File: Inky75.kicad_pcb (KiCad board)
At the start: 2 copper layers, 309.5 x 152.1 mm, 193 parts, among them J1 J, K1 K, M1 M, P1 P, Q1 Q, T1 T, U1 KB2040, U2 U, X1 X, Y1 Y

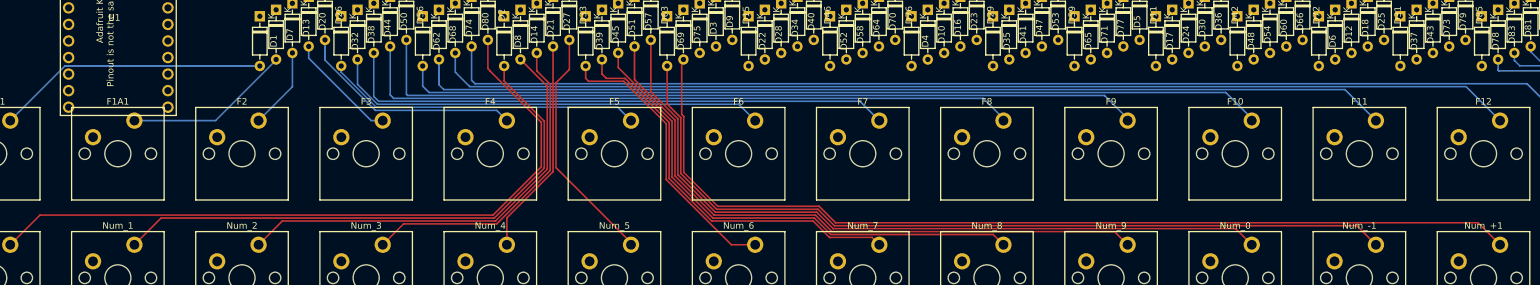
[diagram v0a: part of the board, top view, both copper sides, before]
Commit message: started tidying traces
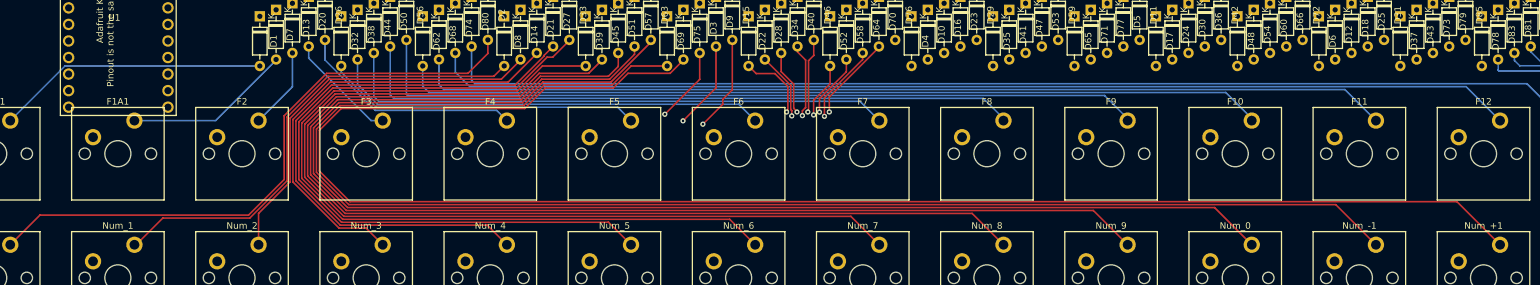
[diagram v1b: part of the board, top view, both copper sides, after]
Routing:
- net Net-(D75-Pad2): track 147.4 -> 252.5 mm
- net Net-(D69-Pad2): track 128.5 -> 231.6 mm
- net Net-(D63-Pad2): track 114.9 -> 213.0 mm
- net Net-(D57-Pad2): track 96.3 -> 192.7 mm
- net Net-(D51-Pad2): track 77.6 -> 172.4 mm
- net Net-(D45-Pad2): track 60.7 -> 150.4 mm
- net Net-(D39-Pad2): track 43.5 -> 129.5 mm
- net Net-(D33-Pad2): track 37.0 -> 110.7 mm
- net Net-(D27-Pad2): track 33.4 -> 89.9 mm
- net Net-(D21-Pad2): track 49.3 -> 69.0 mm
- net Net-(D2-Pad2): track 109.3 -> 93.2 mm
- net Net-(D15-Pad2): track 0.00 -> 14.8 mm, vias 0 -> 1
- net Net-(D9-Pad2): track 0.00 -> 13.5 mm, vias 0 -> 1
- net Net-(D70-Pad2): track 0.00 -> 13.2 mm, vias 0 -> 1
- net Net-(D64-Pad2): track 0.00 -> 12.1 mm, vias 0 -> 1
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
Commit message: fixing traces
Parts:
- removed the D43 at (292.1, 78.7)
- added D78: 1N4148, Diode_THT:D_DO-35_SOD27_P7.62mm_Horizontal, F.Cu at (277.1, 79.7)
- moved D31 4.72 mm to (289.6, 79.7)
- moved D12 2.69 mm to (282.1, 77.7)
- moved D18 2.69 mm to (284.6, 76.7)
- moved D25 2.69 mm to (287.1, 75.7)
- moved D37 2.69 mm to (292.1, 78.7)
- moved D6 2.69 mm to (279.6, 78.7)
- renumbered D73 to D43, D79 to D73, D85 to D79, D78 to D85
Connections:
- D43 pad 2: Net-(D73-Pad2) -> Net-(D43-Pad2)
- D46 pad 1: unconnected-(D46-Pad1) -> Row_3
- D46 pad 2: unconnected-(D46-Pad2) -> Net-(D46-Pad2)
- D73 pad 2: Net-(D79-Pad2) -> Net-(D73-Pad2)
- D79 pad 2: Net-(D85-Pad2) -> Net-(D79-Pad2)
- D85 pad 1: Row_5 -> Row_6
- D85 pad 2: Net-(D78-Pad2) -> Net-(D85-Pad2)
- U2 pad 2: unconnected-(U2-Pad2) -> Net-(D46-Pad2)
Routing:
- net Col_11: track 0.00 -> 359.1 mm, vias 0 -> 1
- net Col_14: track 0.00 -> 330.8 mm
- net Net-(D6-Pad2): track 2.38 -> 332.6 mm, vias 0 -> 2
- net Net-(D12-Pad2): track 7.14 -> 308.5 mm, vias 0 -> 2
- net Net-(D5-Pad2): track 0.00 -> 296.3 mm, vias 0 -> 2
- net Col_9: track 0.00 -> 293.1 mm, vias 0 -> 1
- net Col_13: track 0.00 -> 279.3 mm
- net Net-(D18-Pad2): track 9.52 -> 282.9 mm, vias 0 -> 2
- net Net-(D11-Pad2): track 0.00 -> 268.7 mm, vias 0 -> 2
- net Col_10: track 0.00 -> 259.0 mm, vias 0 -> 1
- net Col_8: track 0.00 -> 250.9 mm, vias 0 -> 1
- net Net-(D17-Pad2): track 0.00 -> 249.0 mm, vias 0 -> 2
- net Net-(C1-Pad2): track 0.00 -> 232.5 mm, vias 0 -> 2
- net Col_7: track 0.00 -> 231.0 mm
- net Net-(D30-Pad2): track 0.00 -> 216.0 mm, vias 0 -> 2
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
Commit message: finished routing traces
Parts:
- removed U$1, U$17, U$19, U$21: MOUNTINGHOLE2.5, Adafruit 1.3in 128x64 OLED STEMMA QT:MOUNTINGHOLE_2.5_PLATED
- removed U$25: , Adafruit 1.3in 128x64 OLED STEMMA QT:PCBFEAT-REV-040
- removed U1: KB2040, kb2040_NEW:KB2040_FINAAL
- added J2: helios_border, 0xCB-HeliosFootprint:helios_border, F.Cu at (93.4, 74.9)
- moved D1 2.36 mm to (114.6, 77.4)
- moved D10 2.36 mm to (222.1, 74.4)
- moved D11 2.36 mm to (257.1, 75.4)
- moved D12 2.36 mm to (294.6, 75.4)
- moved D13 2.36 mm to (119.6, 75.4)
- moved D14 2.36 mm to (154.6, 76.4)
- moved D15 2.36 mm to (189.6, 77.4)
- moved D16 2.36 mm to (224.6, 73.4)
- moved D17 2.36 mm to (259.6, 74.4)
- moved D18 2.36 mm to (297.1, 74.4)
- moved D2 2.36 mm to (149.6, 73.4)
- moved D20 2.36 mm to (122.1, 74.4)
- moved D21 2.36 mm to (157.1, 75.4)
- moved D22 2.36 mm to (192.1, 76.4)
- moved D23 2.36 mm to (227.1, 77.4)
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- renumbered D23 to D10, D30 to D11, D43 to D12, D22 to D15, D29 to D16, D36 to D17, D73 to D18, D28 to D22, D35 to D23, D42 to D24, D79 to D25, D34 to D28, D41 to D29, D9 to D3, D48 to D30, D85 to D31, D40 to D34, D47 to D35, D54 to D36, D83 to D37, D16 to D4, D46 to D40, D53 to D41, D60 to D42, D81 to D43, D52 to D46, D59 to D47, D66 to D48, D84 to D49, D24 to D5, D58 to D52, D65 to D53, D72 to D54, D67 to D55, D64 to D58, D71 to D59, D37 to D6, D78 to D60, D31 to D61, D70 to D64, D77 to D65, D6 to D66, D61 to D67, D76 to D70, D5 to D71, D12 to D72, D82 to D73, D4 to D76, D11 to D77, D18 to D78, D49 to D79, D17 to D81, D10 to D82, D3 to D83, D25 to D84, D55 to D85, D15 to D9
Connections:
- D10 pad 2: Net-(D19-Pad2) -> Net-(A1-Pad2)
- D11 pad 2: Net-(D30-Pad2) -> Net-(D11-Pad2)
- D12 pad 2: Net-(D43-Pad2) -> Net-(D12-Pad2)
- D15 pad 2: Net-(D22-Pad2) -> Net-(D15-Pad2)
- D16 pad 2: Net-(D29-Pad2) -> Net-(D16-Pad2)
- D17 pad 2: Net-(B1-Pad2) -> Net-(D17-Pad2)
- D18 pad 2: Net-(D73-Pad2) -> Net-(D18-Pad2)
- D22 pad 2: Net-(D28-Pad2) -> Net-(D22-Pad2)
- D23 pad 2: Net-(D35-Pad2) -> Net-(D19-Pad2)
- D24 pad 2: Net-(D42-Pad2) -> Net-(C1-Pad2)
- D25 pad 2: Net-(D79-Pad2) -> Net-(D25-Pad2)
- D28 pad 2: Net-(D34-Pad2) -> Net-(D28-Pad2)
- D29 pad 2: Net-(D41-Pad2) -> Net-(D29-Pad2)
- D3 pad 2: Net-(D9-Pad2) -> Net-(D3-Pad2)
- D30 pad 2: Net-(D48-Pad2) -> Net-(D30-Pad2)
- D31 pad 2: Net-(D85-Pad2) -> Net-(D31-Pad2)
- D34 pad 2: Net-(D40-Pad2) -> Net-(D34-Pad2)
- D35 pad 2: Net-(D47-Pad2) -> Net-(D35-Pad2)
- D36 pad 2: Net-(<1-Pad2) -> Net-(B1-Pad2)
- D37 pad 1: Row_2 -> Row_6
- D37 pad 2: Net-(BACKSPACE1-Pad2) -> Net-(D37-Pad2)
- D4 pad 2: Net-(D16-Pad2) -> Net-(Caps1-Pad2)
- D40 pad 2: Net-(D46-Pad2) -> Net-(D40-Pad2)
- D41 pad 2: Net-(D53-Pad2) -> Net-(D41-Pad2)
- D42 pad 2: Net-(>1-Pad2) -> Net-(D42-Pad2)
- D43 pad 1: Row_4 -> Row_6
- D43 pad 2: Net-(D81-Pad2) -> Net-(D43-Pad2)
- D46 pad 2: Net-(D52-Pad2) -> Net-(D46-Pad2)
- D47 pad 2: Net-(D59-Pad2) -> Net-(D47-Pad2)
- D48 pad 2: Net-(/1-Pad2) -> Net-(D48-Pad2)
- D49 pad 1: Row_5 -> Row_6
- D49 pad 2: Net-(D84-Pad2) -> Net-(D49-Pad2)
- D5 pad 2: Net-(C1-Pad2) -> Net-(D5-Pad2)
- D52 pad 2: Net-(D58-Pad2) -> Net-(D52-Pad2)
- D53 pad 2: Net-(;1-Pad2) -> Net-(D53-Pad2)
- D54 pad 2: Net-(D72-Pad2) -> Net-(<1-Pad2)
- D55 pad 2: Net-(D67-Pad2) -> Net-(D55-Pad2)
- D58 pad 2: Net-(D64-Pad2) -> Net-(D58-Pad2)
- D59 pad 2: Net-('1-Pad2) -> Net-(D59-Pad2)
- D6 pad 2: Net-(D37-Pad2) -> Net-(D6-Pad2)
- D60 pad 2: Net-(D78-Pad2) -> Net-(>1-Pad2)
- D61 pad 2: Net-(D31-Pad2) -> Net-(D61-Pad2)
- D64 pad 2: Net-(D70-Pad2) -> Net-(D64-Pad2)
- D65 pad 2: Net-(D77-Pad2) -> Net-(;1-Pad2)
- D66 pad 1: Row_6 -> Row_5
- D66 pad 2: Net-(D6-Pad2) -> Net-(/1-Pad2)
- D67 pad 2: Net-(D61-Pad2) -> Net-(D67-Pad2)
- D70 pad 2: Net-(D76-Pad2) -> Net-(D70-Pad2)
- D71 pad 1: Row_5 -> Row_4
- D71 pad 2: Net-(D5-Pad2) -> Net-('1-Pad2)
- D72 pad 1: Row_6 -> Row_5
- D72 pad 2: Net-(D12-Pad2) -> Net-(D72-Pad2)
- D73 pad 1: Row_3 -> Row_6
- D73 pad 2: Net-(D82-Pad2) -> Net-(D73-Pad2)
- D76 pad 1: Row_4 -> Row_3
- D76 pad 2: Net-(Caps1-Pad2) -> Net-(D76-Pad2)
- D77 pad 1: Row_5 -> Row_4
- D77 pad 2: Net-(D11-Pad2) -> Net-(D77-Pad2)
- D78 pad 1: Row_6 -> Row_5
- D78 pad 2: Net-(D18-Pad2) -> Net-(D78-Pad2)
- D79 pad 2: Net-(D49-Pad2) -> Net-(D79-Pad2)
- D81 pad 1: Row_5 -> Row_4
- D81 pad 2: Net-(D17-Pad2) -> Net-(D81-Pad2)
- D82 pad 1: Row_4 -> Row_3
- D82 pad 2: Net-(A1-Pad2) -> Net-(D82-Pad2)
- D83 pad 1: Row_3 -> Row_2
- D83 pad 2: Net-(D3-Pad2) -> Net-(BACKSPACE1-Pad2)
- D84 pad 1: Row_6 -> Row_5
- D84 pad 2: Net-(D25-Pad2) -> Net-(D84-Pad2)
- D85 pad 2: Net-(D55-Pad2) -> Net-(D85-Pad2)
- D9 pad 2: Net-(D15-Pad2) -> Net-(D9-Pad2)
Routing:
- net Net-(BACKSPACE1-Pad2): track 49.3 -> 285.2 mm
- net Row_6: track 30.5 -> 234.1 mm
- net Col_10: track 259.0 -> 424.6 mm, vias 1 -> 2
- net Col_12: track 153.3 -> 312.0 mm, vias 0 -> 1
- net Row_5: track 41.3 -> 194.2 mm
- net Col_8: track 250.9 -> 376.9 mm, vias 1 -> 2
- net Net-(D81-Pad2): track 78.9 -> 204.1 mm, vias 0 -> 2
- net Row_4: track 39.2 -> 158.7 mm
- net Col_9: track 293.1 -> 402.1 mm, vias 1 -> 2
- net Net-(D82-Pad2): track 38.6 -> 130.8 mm
- net Col_11: track 359.1 -> 444.4 mm, vias 1 -> 2
- net Row_3: track 39.2 -> 124.2 mm
- net Col_14: track 330.8 -> 386.0 mm, vias 0 -> 1
- net Col_13: track 279.3 -> 332.5 mm, vias 0 -> 1
- net Row_2: track 41.3 -> 91.7 mm
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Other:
- board size 309.5 x 152.1 mm -> 309.5 x 146 mm

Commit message: updated traces
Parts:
- removed the ? at (368.3, 92.1)
- removed L_ALT1.5u1: L_ALT_1.5u, Switch_Keyboard_Cherry_MX:SW_Cherry_MX_PCB_1.50u
- removed L_CTRL1: L_CTRL, Switch_Keyboard_Cherry_MX:SW_Cherry_MX_PCB_1.25u
- removed L_SUPER_1.5u1: L_SUPER_1.5u, Switch_Keyboard_Cherry_MX:SW_Cherry_MX_PCB_1.50u
- removed the REF** at (350.0, 110.3)
- removed the REF** at (350.0, 148.4)
- removed R_SPACEBAR2_2.75u1: R_SPACEBAR2_2.75u, Switch_Keyboard_Cherry_MX:SW_Cherry_MX_PCB_2.75u
- added D49: 1N4148, Diode_THT:D_DO-35_SOD27_P7.62mm_Horizontal, F.Cu at (324.6, 73.4)
- added REF**: Stabilizer_Cherry_MX_2.00u, Mounting_Keyboard_Stabilizer:Stabilizer_Cherry_MX_2.00u, F.Cu at (166.7, 196.0)
- added REF**: Stabilizer_Cherry_MX_3.00u, Mounting_Keyboard_Stabilizer:Stabilizer_Cherry_MX_3.00u, F.Cu at (169.1, 196.0)
- added REF**: Stabilizer_Cherry_MX_3.00u, Mounting_Keyboard_Stabilizer:Stabilizer_Cherry_MX_3.00u, F.Cu at (226.2, 196.0)
- added REF**: Stabilizer_Cherry_MX_6.00u, Mounting_Keyboard_Stabilizer:Stabilizer_Cherry_MX_6.00u, F.Cu at (197.6, 196.0)
- added REF**: Stabilizer_Cherry_MX_2.00u, Mounting_Keyboard_Stabilizer:Stabilizer_Cherry_MX_2.00u, F.Cu at (85.7, 177.0)
- added REF**: Stabilizer_Cherry_MX_2.00u, Mounting_Keyboard_Stabilizer:Stabilizer_Cherry_MX_2.00u, F.Cu at (331.0, 119.8)
- added REF**: Stabilizer_Cherry_MX_2.00u, Mounting_Keyboard_Stabilizer:Stabilizer_Cherry_MX_2.00u, F.Cu at (235.7, 196.0)
- added REF**: Stabilizer_Cherry_MX_2.00u, Mounting_Keyboard_Stabilizer:Stabilizer_Cherry_MX_2.00u, F.Cu at (338.1, 148.4)
- added R_SPACEBAR2_2.00u1: R_SPACEBAR2_2.00u1, Switch_Keyboard_Cherry_MX:SW_Cherry_MX_PCB_2.00u, F.Cu at (235.7, 196.0)
- added SPACEBAR1_1.25u3: SPACEBAR1_1.25u3, Switch_Keyboard_Cherry_MX:SW_Cherry_MX_PCB_1.25u, F.Cu at (204.8, 196.0)
- added SW1: SW_Push, Button_Switch_SMD:SW_SPST_TL3342, B.Cu at (110.3, 67.5)
- J2: value helios_border -> helios; footprint 0xCB-HeliosFootprint:helios_border -> 0xCB-HeliosFootprint:helios_no_GP_25
- L_ALT1: footprint Switch_Keyboard_Cherry_MX:SW_Cherry_MX_PCB_1.25u -> Switch_Keyboard_Cherry_MX:SW_Cherry_MX_PCB_1.00u
- L_SPACEBAR1: value L_SPACEBAR -> L_SPACEBAR_1_3u
- SPACEBAR_2: value SPACEBAR_2 -> SPACEBAR_2_3u
- moved L_SPACEBAR1_2.75u1 9.52 mm to (166.7, 196.0)
- moved ? 5.56 mm to (65.1, 59.5)
- moved REF** 5.56 mm to (65.1, 59.5)
- moved L_ALT1 2.38 mm to (102.4, 196.0)
- moved J2 0.34 mm to (93.4, 74.6)
- renumbered D37 to D31, D43 to D37, D73 to D43, D49 to D55, D55 to D67, D79 to D73, D85 to D79, D67 to D85, D31 to D86
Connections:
- D31 pad 2: Net-(D37-Pad2) -> Net-(D31-Pad2)
- D37 pad 2: Net-(D43-Pad2) -> Net-(D37-Pad2)
- D43 pad 2: Net-(D73-Pad2) -> Net-(D43-Pad2)
- D55 pad 2: Net-(D49-Pad2) -> Net-(D55-Pad2)
- D67 pad 2: Net-(D55-Pad2) -> Net-(D67-Pad2)
- D73 pad 2: Net-(D79-Pad2) -> Net-(D73-Pad2)
- D79 pad 2: Net-(D85-Pad2) -> Net-(D79-Pad2)
- D85 pad 2: Net-(D67-Pad2) -> Net-(D85-Pad2)
- D86 pad 2: Net-(D31-Pad2) -> Net-(D86-Pad2)
- J2 pad 10: Row_3 -> Col_13
- J2 pad 11: Row_2 -> Col_12
- J2 pad 12: Row_1 -> Col_11
- J2 pad 13: Col_1 -> Col_10
- J2 pad 14: Col_2 -> Col_9
- J2 pad 15: Col_3 -> Col_8
- J2 pad 16: Col_14 -> Col_7
- J2 pad 17: Col_13 -> Col_6
- J2 pad 18: Col_12 -> Col_5
- J2 pad 19: Col_11 -> Col_4
- J2 pad 20: Col_10 -> Col_15
- J2 pad 21: Col_9 -> Row_1
- J2 pad 22: Col_8 -> Row_2
- J2 pad 23: Col_7 -> Row_3
- J2 pad 24: Col_6 -> Row_4
- J2 pad 25: Col_5 -> Row_5
- J2 pad 26: Col_4 -> Row_6
- J2 pad 28: unconnected-(J2-Pad28) -> RST
- J2 pad 29: unconnected-(J2-Pad29) -> GND
- J2 pad 6: unconnected-(J2-Pad6) -> Col_1
- J2 pad 7: Row_6 -> Col_2
- J2 pad 8: Row_5 -> Col_3
- J2 pad 9: Row_4 -> Col_14
- SPACEBAR1_6u1 pad 1: Col_4 -> Col_15
- SPACEBAR1_6u1 pad 2: Net-(D25-Pad2) -> Net-(D86-Pad2)
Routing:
- net Net-(D86-Pad2): track 0.00 -> 216.5 mm, vias 0 -> 2
- net Col_15: track 0.00 -> 174.1 mm
- net Col_9: track 402.1 -> 373.4 mm
- net Col_10: track 424.6 -> 396.2 mm
- net Col_14: track 386.0 -> 413.2 mm
- net Col_13: track 332.5 -> 358.3 mm
- net Col_8: track 376.9 -> 352.4 mm
- net Col_12: track 312.0 -> 336.4 mm
- net Col_11: track 444.4 -> 420.4 mm
- net Col_3: track 131.5 -> 154.4 mm
- net Col_2: track 118.0 -> 140.6 mm
- net Col_4: track 188.4 -> 166.9 mm
- net Col_1: track 123.3 -> 143.9 mm
- net Col_7: track 270.0 -> 286.5 mm
- net Col_6: track 238.0 -> 254.5 mm
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- added copper zone on B.Cu, net GND
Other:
- board size 309.5 x 146 mm -> 309.5 x 151.6 mm
